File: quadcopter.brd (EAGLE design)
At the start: 133.6 x 133.6 mm, 65 parts, among them J1 AVR_SPI_PRG_6NS, Q1 N-CHANNEL_MOSFET, Q2 N-CHANNEL_MOSFET, Q3 N-CHANNEL_MOSFET, Q4 N-CHANNEL_MOSFET, U1 ATMEGA128RFA1

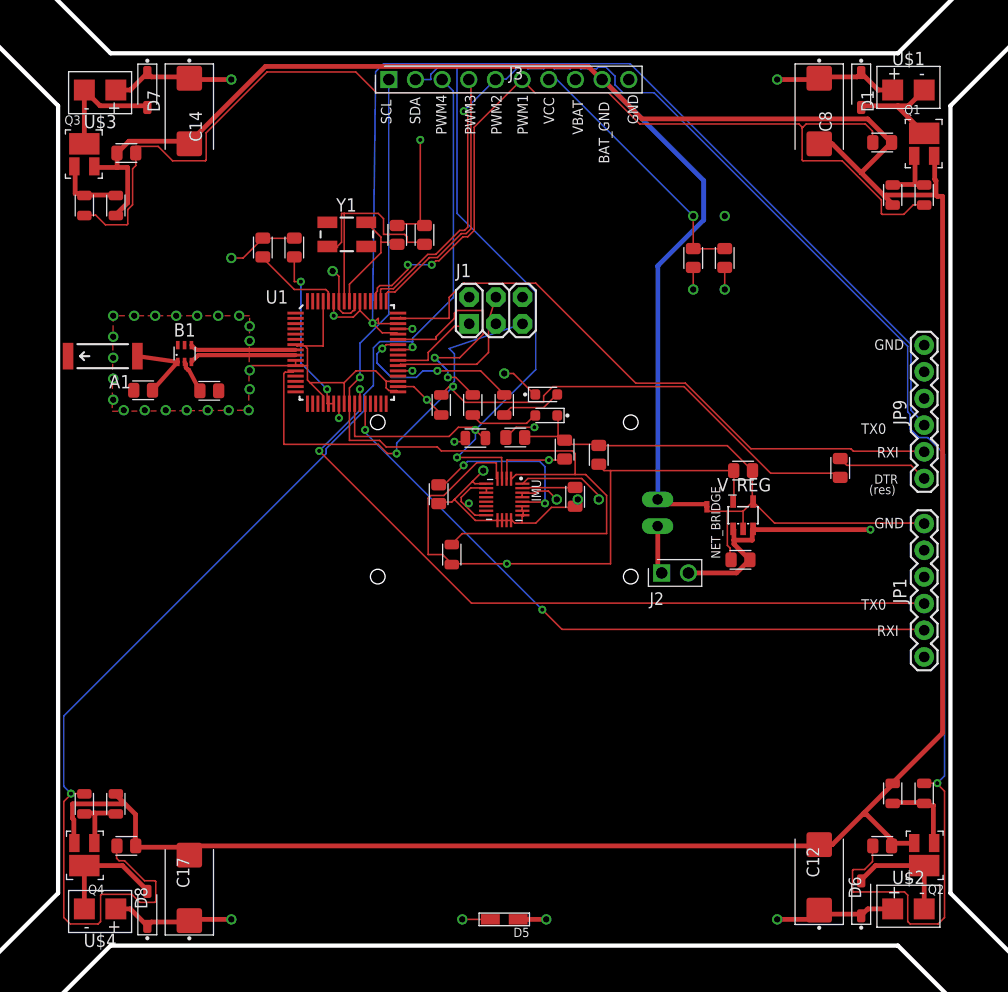
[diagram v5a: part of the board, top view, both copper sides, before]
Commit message: Commiting before the autorouter ruins e verything
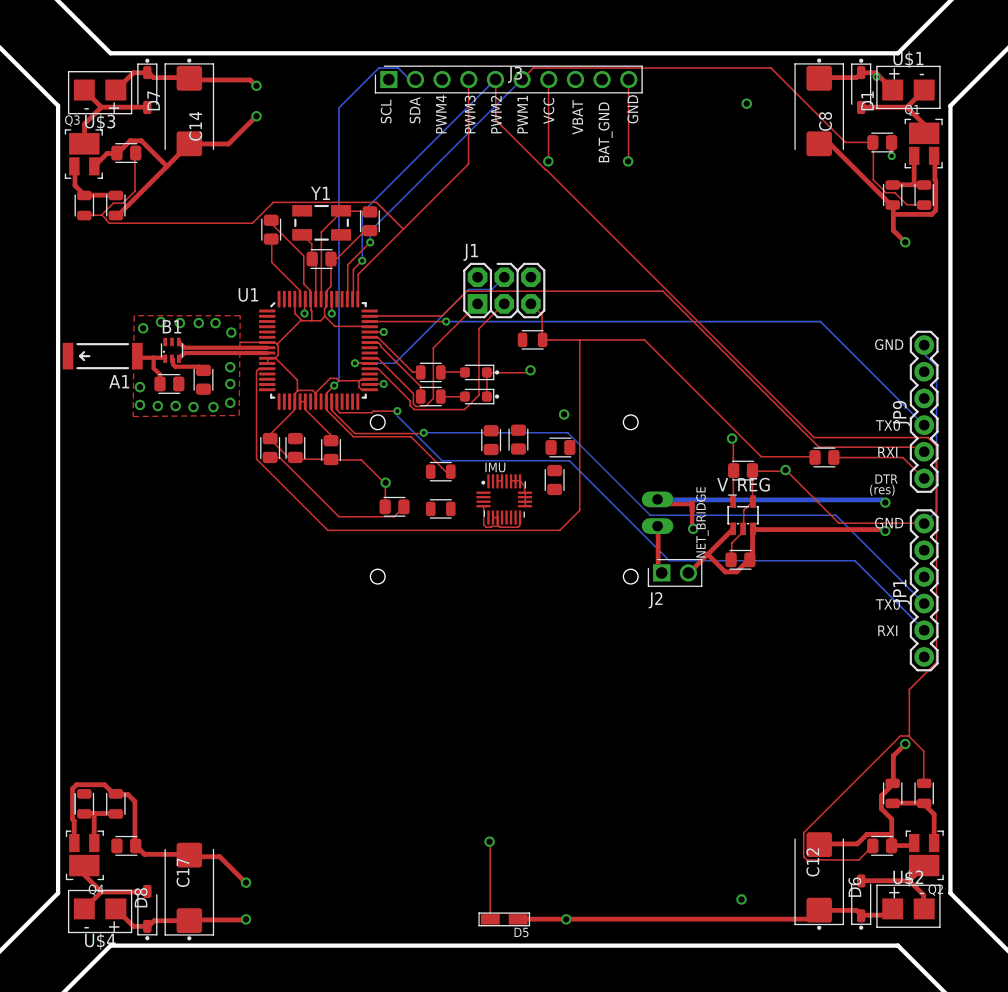
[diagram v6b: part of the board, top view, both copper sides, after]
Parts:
- moved C3 44.7 mm to (50.1, 74.9)
- moved C4 44.2 mm to (47.7, 74.9), turned to 270 degrees
- moved C22 20.1 mm to (59.5, 69.3), turned to 180 degrees
- moved C2 19.6 mm to (53.5, 74.7), turned to 270 degrees
- moved R1 10.7 mm to (72.7, 85.2), turned to 0 degrees
- moved C5 10.1 mm to (52.6, 92.9), turned to 0 degrees
- moved C21 9.65 mm to (68.8, 75.7), turned to 270 degrees
- moved C18 9.21 mm to (71.3, 75.7)
- moved LED2 7.85 mm to (67.3, 82.1)
- moved R5 7.05 mm to (63.0, 79.8), turned to 180 degrees
- moved LED3 6.70 mm to (67.3, 79.8), turned to 180 degrees
- moved C19 5.52 mm to (74.8, 71.8), turned to 270 degrees
- moved R6 5.06 mm to (63.0, 82.1), turned to 180 degrees
- moved R13 4.60 mm to (64.0, 72.7)
- moved R12 4.47 mm to (64.0, 69.1), turned to 180 degrees
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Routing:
- net BAT_GND: track 318.6 -> 124.6 mm, vias 0 -> 6
- net PWM4: track 121.1 -> 0.00 mm, vias 2 -> 0
- net SCL: track 88.9 -> 0.00 mm, vias 1 -> 0
- net VCC: track 131.1 -> 42.9 mm, vias 13 -> 6
- net RX0: track 97.6 -> 56.9 mm
- net VBAT: track 75.0 -> 99.8 mm, vias 6 -> 7
- net SDA: track 70.7 -> 53.2 mm, vias 2 -> 1
- net N$1: track 24.0 -> 6.68 mm
- net N$13: track 17.0 -> 0.00 mm, vias 2 -> 0
- net PB7: track 23.0 -> 6.26 mm, vias 2 -> 0
- net PWM2: track 154.7 -> 142.5 mm, vias 2 -> 1
- net RESET: track 82.9 -> 94.6 mm, vias 2 -> 0
- net N$2: track 16.3 -> 5.24 mm, vias 2 -> 0
- net MISO: track 8.68 -> 19.6 mm
- net SCK: track 11.8 -> 22.6 mm, vias 1 -> 0
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- added copper zone on layer 15, net BAT_GND

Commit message: Autorouting complete after review
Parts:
- moved R13 3.71 mm to (63.6, 69.0)
- moved R12 2.42 mm to (63.6, 71.5), turned to 0 degrees
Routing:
- net PWM4: track 0.00 -> 91.7 mm, vias 0 -> 3
- net VCC: track 42.9 -> 134.3 mm
- net SCL: track 0.00 -> 65.1 mm, vias 0 -> 2
- net GND: track 149.4 -> 167.0 mm, vias 22 -> 24
- net VBAT: track 99.8 -> 84.6 mm
- net N$13: track 0.00 -> 5.34 mm
- net SDA: track 53.2 -> 58.0 mm, vias 1 -> 2
- net N$15: track 0.00 -> 3.13 mm
- net RESET: track 94.6 -> 96.9 mm

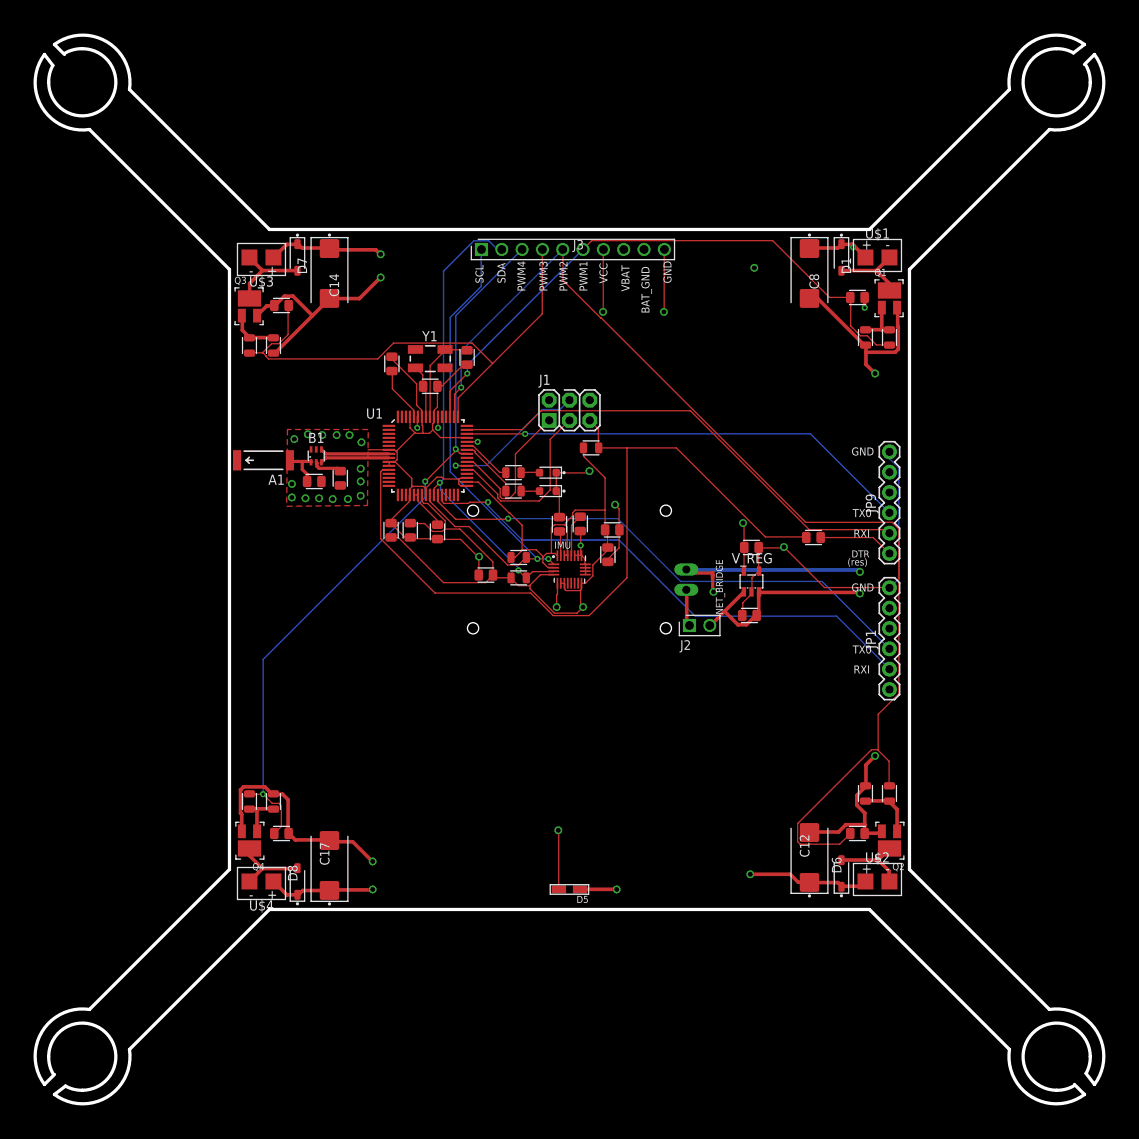
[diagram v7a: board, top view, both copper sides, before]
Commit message: Added additional 2mm to arm lengths"
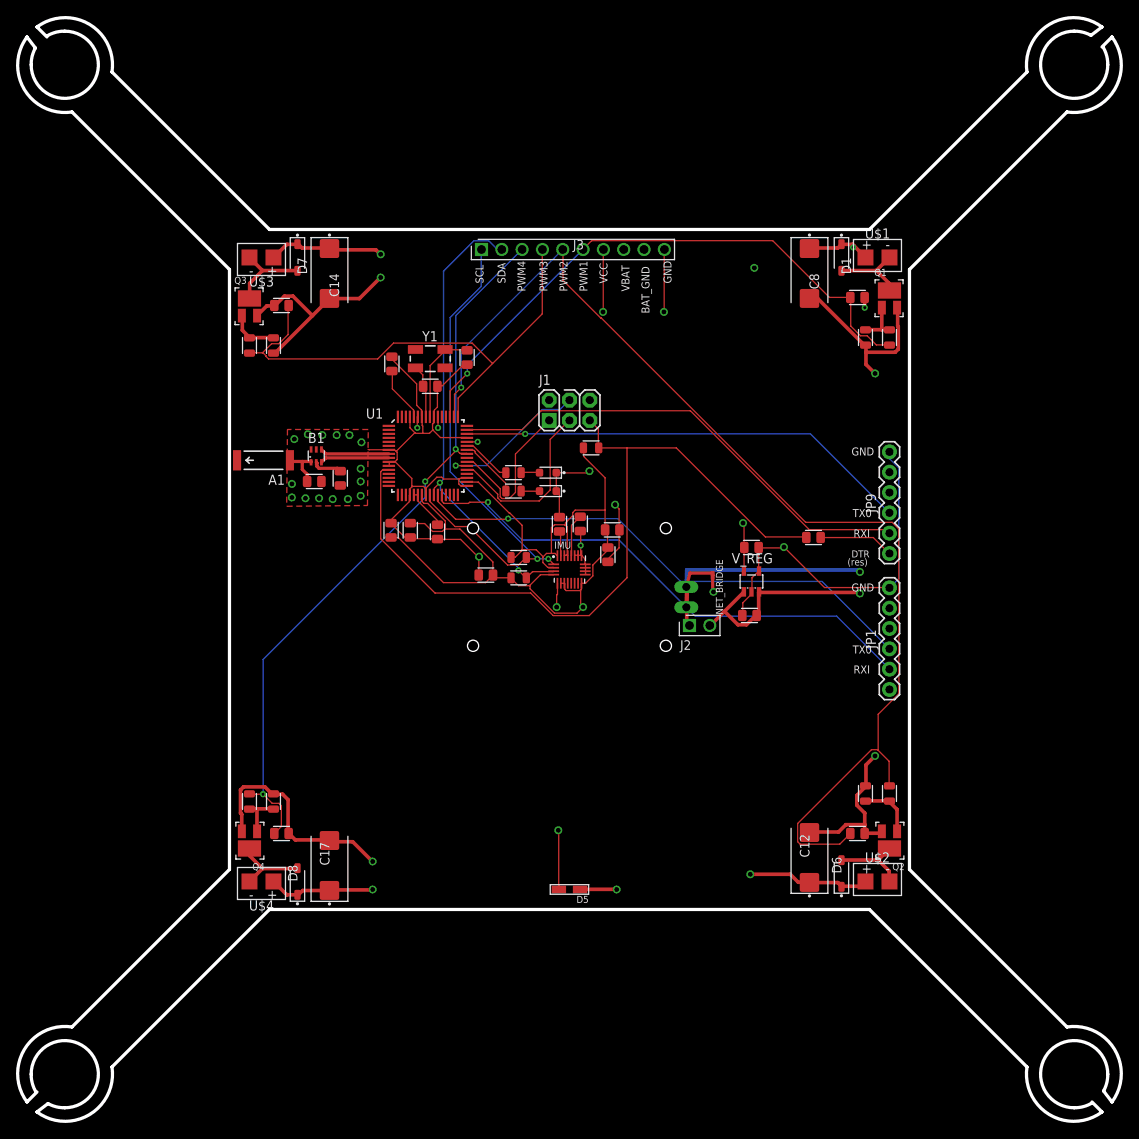
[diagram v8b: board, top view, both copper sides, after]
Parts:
- moved BATT1 2.19 mm to (70.0, 67.8)
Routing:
- net BAT_GND: track 124.6 -> 127.9 mm
- net N$18: track 4.64 -> 6.75 mm
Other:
- board size 133.6 x 133.6 mm -> 138 x 138 mm
